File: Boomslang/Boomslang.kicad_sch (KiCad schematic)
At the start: 99 parts, among them J1 Screw_Terminal_01x04, J2 Screw_Terminal_01x04, J3 Screw_Terminal_01x04, J4 01x04, J5 Screw_Terminal_01x02, J6 Screw_Terminal_01x02, Q1 IRLZ44N, Q10 2N3904, Q11 IRLZ44N, Q12 2N3904, Q13 2N3904, Q14 2N3904, Q15 2N3906, Q16 2N3904, Q17 IRLZ44N, Q18 2N3904, Q19 2N2222A, Q2 2N3904, Q20 2N2222A, Q3 2N3906, Q4 2N3904, Q5 2N3904, Q6 2N3904, Q7 2N3904, Q8 2N3904, Q9 2N3906, U1 L7805

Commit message: Break out GPIO2 battery sense and GPIO12-14 test points
Adds the GPIO2 12V battery-voltage sense (1:11 divider, matches
firmware's PIN_BATTERY/BATTERY_DIVIDER_RATIO) and breaks out
GPIO12-14 as spare test points for timing tests and similar bring-up
work. Regenerated gerbers and schematic/board renders to match.
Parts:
- added C13: 100 pF, Capacitor_THT:C_Disc_D5.0mm_W2.5mm_P5.00mm, symbol Device:C_Small
- added J7: Conn_01x04_Pin, Connector_PinSocket_2.54mm:PinSocket_1x04_P2.54mm_Vertical, symbol Connector:Conn_01x04_Pin
- added R45, R46, R47, R48, R50: 100k, Resistor_THT:R_Axial_DIN0207_L6.3mm_D2.5mm_P7.62mm_Horizontal, symbol Device:R
- added R49: 10k, Resistor_THT:R_Axial_DIN0207_L6.3mm_D2.5mm_P7.62mm_Horizontal, symbol Device:R
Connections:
- net +12V: now also R50.1
- net CONTINUITY1: now also R46.1
- net CONTINUITY2: now also R47.1
- net CONTINUITY3: now also R48.1
- net GND: now also C13.2, J7.4 (Pin_4), R45.2, R46.2, R47.2, R48.2, R49.2
- net SENSEFAILSAFE: now also R45.1
- net at DB1.18 (12): now also J7.1 (Pin_1)
- net at DB1.19 (13): now also J7.2 (Pin_2)
- net at DB1.20 (14): now also J7.3 (Pin_3)
- net PWRSENSE: now reaches DB1.40 (2)
- net PWRSENSE: now also C13.1, R49.1, R50.2

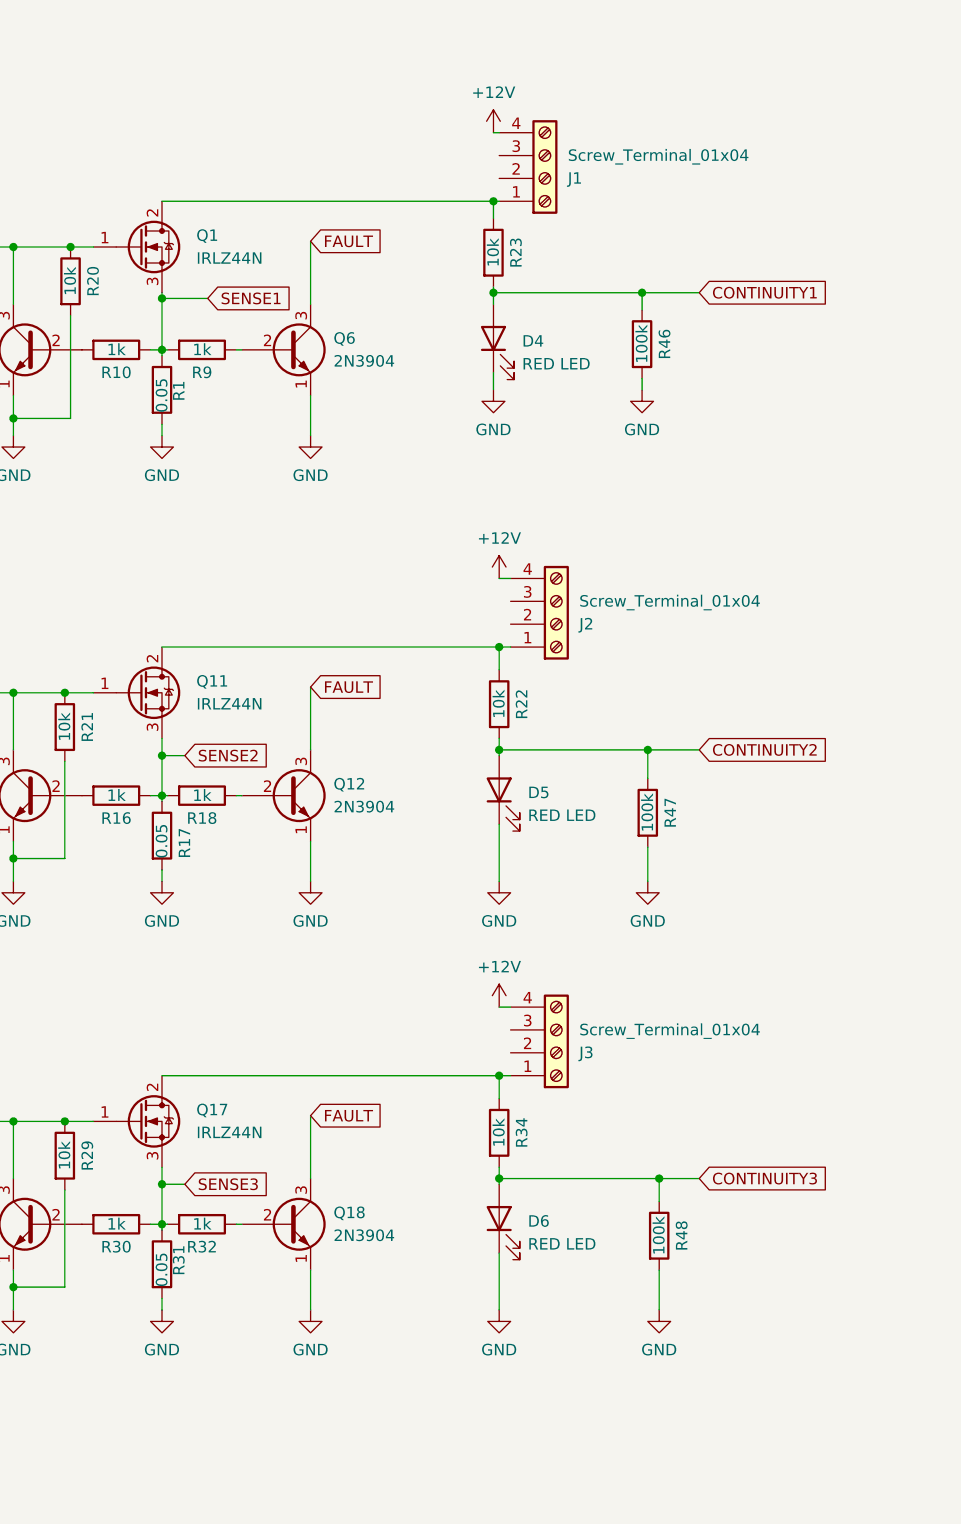
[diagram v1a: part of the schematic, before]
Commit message: Add snubbers to MOSFET drains
RC snubber on each channel's IRLZ44N drain to damp switching
transients from the igniter/wiring inductance. Regenerated gerbers
and schematic/board renders to match.
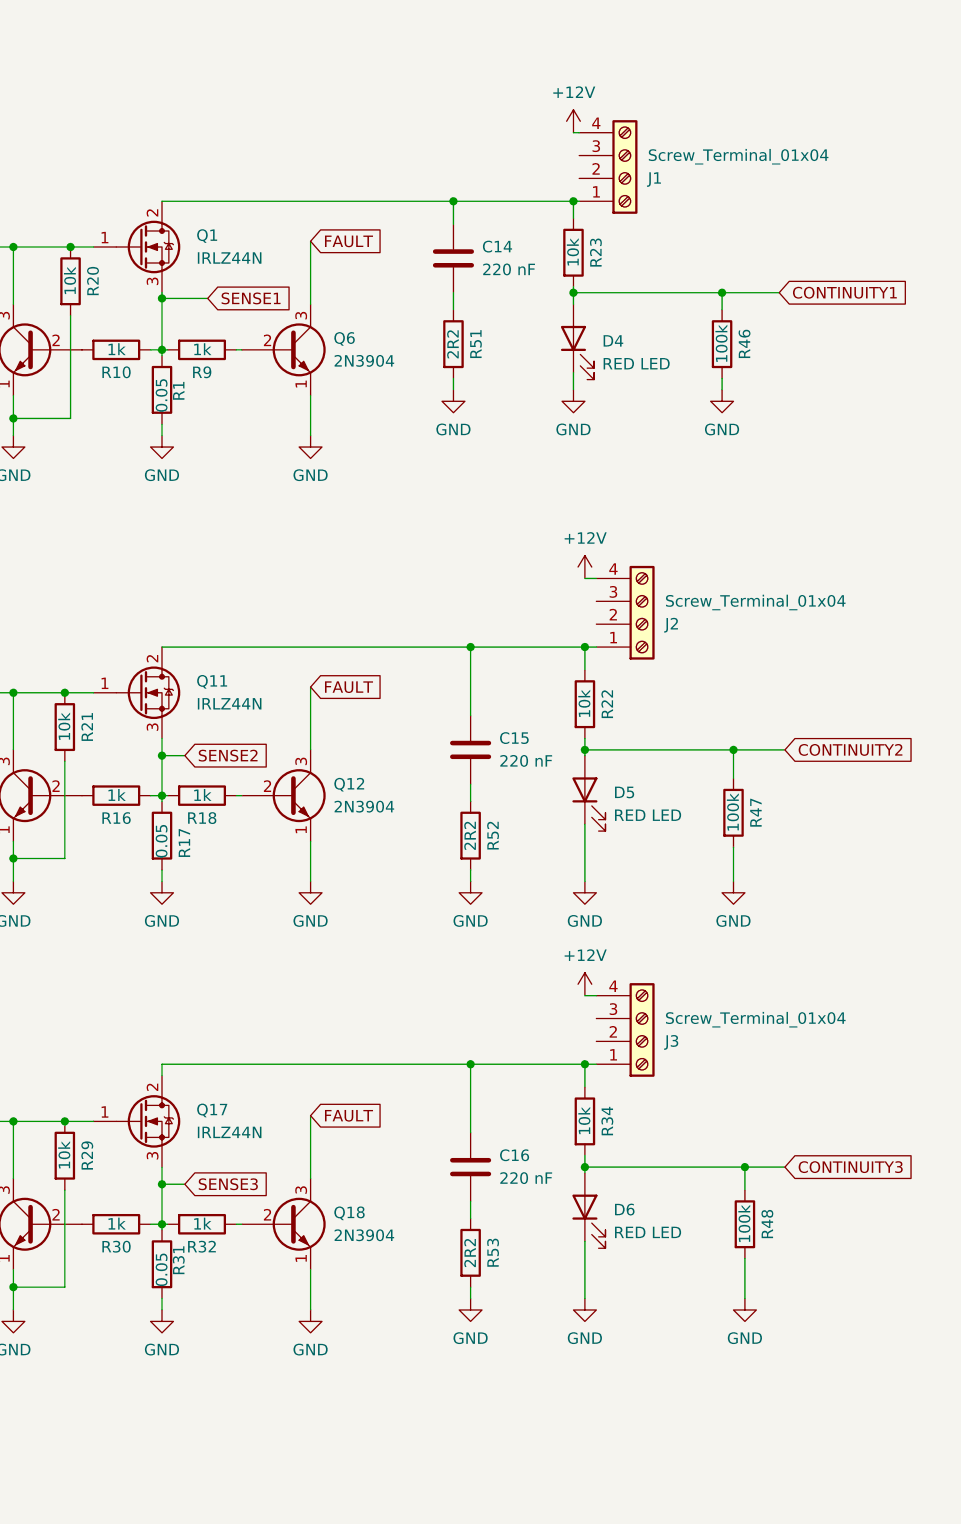
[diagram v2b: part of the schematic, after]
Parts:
- added C14, C15, C16: 220 nF, Capacitor_THT:C_Rect_L7.0mm_W2.5mm_P5.00mm, symbol Device:C
- added R51, R52, R53: 2R2, Resistor_THT:R_Axial_DIN0207_L6.3mm_D2.5mm_P7.62mm_Horizontal, symbol Device:R
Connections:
- net GND: now also R51.2, R52.2, R53.2
- net at J2.1 (Pin_1), Q11.2 (D), R22.1: now also C15.1
- net at J3.1 (Pin_1), Q17.2 (D), R34.1: now also C16.1
- net at J1.1 (Pin_1), Q1.2 (D), R23.1: now also C14.1
- new net: C15.2, R52.1
- new net: C14.2, R51.1
- new net: C16.2, R53.1
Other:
- moved on the sheet: D4, D5, D6, J1, J2, J3, R22, R23, R34, R46, R47, R48

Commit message: Changed snubber resistor footprint
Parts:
- R51, R52, R53: footprint Resistor_THT:R_Axial_DIN0207_L6.3mm_D2.5mm_P7.62mm_Horizontal -> Resistor_THT:R_Axial_DIN0309_L9.0mm_D3.2mm_P12.70mm_Horizontal
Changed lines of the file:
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@@
       (effects (font (size 1.27 1.27)))
     )
-    (property "Footprint" "Resistor_THT:R_Axial_DIN0207_L6.3mm_D2.5mm_P7.62mm_Horizontal" (at 230.632 103.505 90)
+    (property "Footprint" "Resistor_THT:R_Axial_DIN0309_L9.0mm_D3.2mm_P12.70mm_Horizontal" (at 230.632 103.505 90)
       (effects (font (size 1.27 1.27)) hide)
     )
@@
       (effects (font (size 1.27 1.27)))
     )
-    (property "Footprint" "Resistor_THT:R_Axial_DIN0207_L6.3mm_D2.5mm_P7.62mm_Horizontal" (at 230.632 149.86 90)
+    (property "Footprint" "Resistor_THT:R_Axial_DIN0309_L9.0mm_D3.2mm_P12.70mm_Horizontal" (at 230.632 149.86 90)
       (effects (font (size 1.27 1.27)) hide)
     )
@@
       (effects (font (size 1.27 1.27)))
     )
-    (property "Footprint" "Resistor_THT:R_Axial_DIN0207_L6.3mm_D2.5mm_P7.62mm_Horizontal" (at 228.727 48.895 90)
-      (effects (font (size 1.27 1.27)) hide)
-    )
+    (property "Footprint" "Resistor_THT:R_Axial_DIN0309_L9.0mm_D3.2mm_P12.70mm_Horizontal" (at 228.727 48.895 90)
+      (effects (font (size 1.27 1.27)) hide)
+    )

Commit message: Reduce overcurrent comparator base resistor from 1k to 100R
Bench testing (scoped) found the local per-channel overcurrent
comparator's pull-down transistor base resistor was slowing its own
turn-on, letting fault current overshoot well past the ~13A trip
threshold (38A) before the gate was actually pulled down. Reducing the
base resistor from 1k to 100R speeds up that transistor's reaction,
cutting the overshoot to ~15A. Verified in QUCS-S/ngspice simulation
(Simulations/ThresholdTrip) as well as on the bench.

Adds the QUCS-S simulation used to verify this.
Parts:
- R10, R16, R18, R30, R32, R9: value 1k -> 100R
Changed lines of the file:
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@@
       (effects (font (size 1.27 1.27)))
     )
-    (property "Value" "1k" (at 193.04 99.06 90)
+    (property "Value" "100R" (at 193.04 99.06 90)
       (effects (font (size 1.27 1.27)))
     )
@@
       (effects (font (size 1.27 1.27)))
     )
-    (property "Value" "1k" (at 193.04 146.685 90)
+    (property "Value" "100R" (at 193.04 146.685 90)
       (effects (font (size 1.27 1.27)))
     )
@@
       (effects (font (size 1.27 1.27)))
     )
-    (property "Value" "1k" (at 202.565 99.06 90)
+    (property "Value" "100R" (at 202.565 99.06 90)
       (effects (font (size 1.27 1.27)))
     )
@@
       (effects (font (size 1.27 1.27)))
     )
-    (property "Value" "1k" (at 202.565 49.53 90)
+    (property "Value" "100R" (at 202.565 49.53 90)
       (effects (font (size 1.27 1.27)))
     )
@@
       (effects (font (size 1.27 1.27)))
     )
-    (property "Value" "1k" (at 202.565 146.685 90)
+    (property "Value" "100R" (at 202.565 146.685 90)
       (effects (font (size 1.27 1.27)))
     )
@@
       (effects (font (size 1.27 1.27)))
     )
-    (property "Value" "1k" (at 193.04 49.53 90)
+    (property "Value" "100R" (at 193.04 49.53 90)
       (effects (font (size 1.27 1.27)))
     )
